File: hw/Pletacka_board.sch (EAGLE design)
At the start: 52 parts, among them U1 LM75BDP-NEW, U2 EL357N(A)(TA)-G, U3 EL357N(A)(TA)-G, U4 EL357N(A)(TA)-G, U5 EL357N(A)(TA)-G, U6 TPS54231D

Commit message: Start fixing
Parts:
- C1: LCSC_ID (none) -> C13585; LSCS_ID C13585 -> (none)
- D6: LCSC_ID (none) -> C8598; LSCS_ID C8598 -> (none)
- R10, R12, R8: LCSC_ID (none) -> C17944; LSCS_ID C17944 -> (none)

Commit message: Fix all atributes (fix #12)
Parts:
- D1, D2, D4: LCSC_ID (none) -> C8598; LSCS_ID C8598 -> (none)
- R11, R13, R7, R9: LCSC_ID (none) -> C25804; LSCS_ID C25804 -> (none)
- R15: LCSC_ID (none) -> C22818; LSCS_ID C22818 -> (none)
- R6: LCSC_ID (none) -> C17944; LSCS_ID C17944 -> (none)
- S1, S2: LCSC_ID (none) -> C318888
- U$2: LCSC_ID (none) -> C169399
- U2: LCSC_ID (none) -> C6649; LSCS_ID C6649 -> (none)
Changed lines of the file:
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@@
 <part name="CON1" library="#Svorkovnice" deviceset="AK500/2" device=""/>
 <part name="R6" library="rcl_upravena" deviceset="R-EU_" device="R1206" value="2k/0.25W">
-<attribute name="LSCS_ID" value="C17944"/>
+<attribute name="LCSC_ID" value="C17944"/>
 </part>
 <part name="GND6" library="supply1" library_urn="urn:adsk.eagle:library:371" deviceset="GND" device=""/>
 <part name="R7" library="rcl_upravena" deviceset="R-EU_" device="R0603" value="10k">
-<attribute name="LSCS_ID" value="C25804"/>
+<attribute name="LCSC_ID" value="C25804"/>
 </part>
 <part name="+3V3" library="supply1" library_urn="urn:adsk.eagle:library:371" deviceset="+3V3" device=""/>
@@
 <part name="GND7" library="supply1" library_urn="urn:adsk.eagle:library:371" deviceset="GND" device=""/>
 <part name="R9" library="rcl_upravena" deviceset="R-EU_" device="R0603" value="10k">
-<attribute name="LSCS_ID" value="C25804"/>
+<attribute name="LCSC_ID" value="C25804"/>
 </part>
 <part name="+3V4" library="supply1" library_urn="urn:adsk.eagle:library:371" deviceset="+3V3" device=""/>
@@
 <part name="GND8" library="supply1" library_urn="urn:adsk.eagle:library:371" deviceset="GND" device=""/>
 <part name="R11" library="rcl_upravena" deviceset="R-EU_" device="R0603" value="10k">
-<attribute name="LSCS_ID" value="C25804"/>
+<attribute name="LCSC_ID" value="C25804"/>
 </part>
 <part name="+3V5" library="supply1" library_urn="urn:adsk.eagle:library:371" deviceset="+3V3" device=""/>
@@
 <part name="GND9" library="supply1" library_urn="urn:adsk.eagle:library:371" deviceset="GND" device=""/>
 <part name="R13" library="rcl_upravena" deviceset="R-EU_" device="R0603" value="10k">
-<attribute name="LSCS_ID" value="C25804"/>
+<attribute name="LCSC_ID" value="C25804"/>
 </part>
 <part name="+3V6" library="supply1" library_urn="urn:adsk.eagle:library:371" deviceset="+3V3" device=""/>
 <part name="U2" library="EL357N_A__TA_-G" deviceset="EL357N(A)(TA)-G" device="">
-<attribute name="LSCS_ID" value="C6649"/>
+<attribute name="LCSC_ID" value="C6649"/>
 </part>
 <part name="U3" library="EL357N_A__TA_-G" deviceset="EL357N(A)(TA)-G" device="">
@@
 </pinmapping>
 </spice>
-<attribute name="LSCS_ID" value="C22818"/>
+<attribute name="LCSC_ID" value="C22818"/>
 </part>
 <part name="C2" library="rcl_upravena" deviceset="C-EU" device="C0603" value="10p">
@@
 <attribute name="LCSC_ID" value="C2286"/>
 </part>
-<part name="U$2" library="SWRB1204S-680MT" deviceset="SWRB1204S" device=""/>
+<part name="U$2" library="SWRB1204S-680MT" deviceset="SWRB1204S" device="">
+<attribute name="LCSC_ID" value="C169399"/>
+</part>
 <part name="GND12" library="supply1" library_urn="urn:adsk.eagle:library:371" deviceset="GND" device=""/>
-<part name="S1" library="switch-omron" deviceset="10-XX" device="_SMD" value="CHOOSE_ME"/>
-<part name="S2" library="switch-omron" deviceset="10-XX" device="_SMD" value="CHOOSE_ME"/>
+<part name="S1" library="switch-omron" deviceset="10-XX" device="_SMD" value="CHOOSE_ME">
+<attribute name="LCSC_ID" value="C318888"/>
+</part>
+<part name="S2" library="switch-omron" deviceset="10-XX" device="_SMD" value="CHOOSE_ME">
+<attribute name="LCSC_ID" value="C318888"/>
+</part>
 <part name="GND2" library="supply1" library_urn="urn:adsk.eagle:library:371" deviceset="GND" device=""/>
 <part name="+3V7" library="supply1" library_urn="urn:adsk.eagle:library:371" deviceset="+3V3" device=""/>
@@
 </part>
 <part name="D1" library="B5819W" deviceset="B5819W" device="">
-<attribute name="LSCS_ID" value="C8598"/>
+<attribute name="LCSC_ID" value="C8598"/>
 </part>
 <part name="D2" library="B5819W" deviceset="B5819W" device="">
-<attribute name="LSCS_ID" value="C8598"/>
+<attribute name="LCSC_ID" value="C8598"/>
 </part>
 <part name="D4" library="B5819W" deviceset="B5819W" device="">
-<attribute name="LSCS_ID" value="C8598"/>
+<attribute name="LCSC_ID" value="C8598"/>
 </part>
 </parts>
@@
 <instance part="S1" gate="1" x="208.28" y="91.44" smashed="yes" rot="MR270">
 <attribute name="NAME" x="208.28" y="96.52" size="1.27" layer="95" rot="R180" align="top-center"/>
+<attribute name="LCSC_ID" x="208.28" y="91.44" size="1.778" layer="96" rot="MR270" display="off"/>
 </instance>
 <instance part="S2" gate="1" x="208.28" y="60.96" smashed="yes" rot="MR270">
 <attribute name="NAME" x="208.28" y="66.04" size="1.27" layer="95" rot="R180" align="top-center"/>
+<attribute name="LCSC_ID" x="208.28" y="60.96" size="1.778" layer="96" rot="MR270" display="off"/>
 </instance>
 <instance part="GND2" gate="1" x="96.52" y="43.18" smashed="yes" rot="R270">
@@
 <attribute name="NAME" x="29.21" y="151.3586" size="1.778" layer="95"/>
 <attribute name="VALUE" x="29.21" y="146.558" size="1.778" layer="96"/>
-<attribute name="LSCS_ID" x="33.02" y="149.86" size="1.778" layer="96" display="off"/>
+<attribute name="LCSC_ID" x="33.02" y="149.86" size="1.778" layer="96" display="off"/>
 </instance>
 <instance part="GND6" gate="1" x="76.2" y="139.7" smashed="yes">
@@
 <attribute name="NAME" x="74.7014" y="153.67" size="1.778" layer="95" rot="R90"/>
 <attribute name="VALUE" x="79.502" y="153.67" size="1.778" layer="96" rot="R90"/>
-<attribute name="LSCS_ID" x="76.2" y="157.48" size="1.778" layer="96" rot="R90" display="off"/>
+<attribute name="LCSC_ID" x="76.2" y="157.48" size="1.778" layer="96" rot="R90" display="off"/>
 </instance>
 <instance part="+3V3" gate="G$1" x="76.2" y="165.1" smashed="yes">
@@
 <attribute name="NAME" x="74.7014" y="115.57" size="1.778" layer="95" rot="R90"/>
 <attribute name="VALUE" x="79.502" y="115.57" size="1.778" layer="96" rot="R90"/>
-<attribute name="LSCS_ID" x="76.2" y="119.38" size="1.778" layer="96" rot="R90" display="off"/>
+<attribute name="LCSC_ID" x="76.2" y="119.38" size="1.778" layer="96" rot="R90" display="off"/>
 </instance>
 <instance part="+3V4" gate="G$1" x="76.2" y="127" smashed="yes">
@@
 <attribute name="NAME" x="74.7014" y="74.93" size="1.778" layer="95" rot="R90"/>
 <attribute name="VALUE" x="79.502" y="74.93" size="1.778" layer="96" rot="R90"/>
-<attribute name="LSCS_ID" x="76.2" y="78.74" size="1.778" layer="96" rot="R90" display="off"/>
+<attribute name="LCSC_ID" x="76.2" y="78.74" size="1.778" layer="96" rot="R90" display="off"/>
 </instance>
 <instance part="+3V5" gate="G$1" x="76.2" y="86.36" smashed="yes">
@@
 <attribute name="NAME" x="74.7014" y="29.21" size="1.778" layer="95" rot="R90"/>
 <attribute name="VALUE" x="79.502" y="29.21" size="1.778" layer="96" rot="R90"/>
-<attribute name="LSCS_ID" x="76.2" y="33.02" size="1.778" layer="96" rot="R90" display="off"/>
+<attribute name="LCSC_ID" x="76.2" y="33.02" size="1.778" layer="96" rot="R90" display="off"/>
 </instance>
 <instance part="+3V6" gate="G$1" x="76.2" y="40.64" smashed="yes">
@@
 <attribute name="NAME" x="50.7743" y="153.413590625" size="2.08636875" layer="95" ratio="10" rot="SR0"/>
 <attribute name="VALUE" x="50.77441875" y="138.216059375" size="2.087890625" layer="96" ratio="10" rot="SR0"/>
-<attribute name="LSCS_ID" x="58.42" y="147.32" size="1.778" layer="96" display="off"/>
+<attribute name="LCSC_ID" x="58.42" y="147.32" size="1.778" layer="96" display="off"/>
 </instance>
 <instance part="U3" gate="G$1" x="58.42" y="109.22" smashed="yes">
@@
 <attribute name="NAME" x="42.6974" y="111.76" size="1.778" layer="95" rot="R90"/>
 <attribute name="VALUE" x="45.4914" y="111.76" size="1.778" layer="96" rot="R90"/>
-<attribute name="LSCS_ID" x="43.18" y="109.22" size="1.778" layer="96" rot="R90" display="off"/>
+<attribute name="LCSC_ID" x="43.18" y="109.22" size="1.778" layer="96" rot="R90" display="off"/>
 </instance>
 <instance part="D2" gate="G$1" x="43.18" y="68.58" smashed="yes" rot="R90">
 <attribute name="NAME" x="42.6974" y="71.12" size="1.778" layer="95" rot="R90"/>
 <attribute name="VALUE" x="45.4914" y="71.12" size="1.778" layer="96" rot="R90"/>
-<attribute name="LSCS_ID" x="43.18" y="68.58" size="1.778" layer="96" rot="R90" display="off"/>
+<attribute name="LCSC_ID" x="43.18" y="68.58" size="1.778" layer="96" rot="R90" display="off"/>
 </instance>
 <instance part="D4" gate="G$1" x="43.18" y="22.86" smashed="yes" rot="R90">
 <attribute name="NAME" x="42.6974" y="25.4" size="1.778" layer="95" rot="R90"/>
 <attribute name="VALUE" x="45.4914" y="25.4" size="1.778" layer="96" rot="R90"/>
-<attribute name="LSCS_ID" x="43.18" y="22.86" size="1.778" layer="96" rot="R90" display="off"/>
+<attribute name="LCSC_ID" x="43.18" y="22.86" size="1.778" layer="96" rot="R90" display="off"/>
 </instance>
 </instances>
@@
 <attribute name="NAME" x="72.1614" y="74.93" size="1.778" layer="95" rot="R90"/>
 <attribute name="VALUE" x="76.962" y="74.93" size="1.778" layer="96" rot="R90"/>
-<attribute name="LSCS_ID" x="73.66" y="78.74" size="1.778" layer="96" rot="R90" display="off"/>
+<attribute name="LCSC_ID" x="73.66" y="78.74" size="1.778" layer="96" rot="R90" display="off"/>
 </instance>
 <instance part="C2" gate="G$1" x="86.36" y="63.5" smashed="yes">
@@
 <attribute name="LCSC_ID" x="111.76" y="63.5" size="1.778" layer="96" display="off"/>
 </instance>
-<instance part="U$2" gate="G$1" x="208.28" y="83.82" smashed="yes"/>
+<instance part="U$2" gate="G$1" x="208.28" y="83.82" smashed="yes">
+<attribute name="LCSC_ID" x="208.28" y="83.82" size="1.778" layer="96" display="off"/>
+</instance>
 <instance part="D3" gate="G$1" x="190.5" y="96.52" smashed="yes" rot="R270">
 <attribute name="NAME" x="192.405" y="98.806" size="1.27" layer="95" rot="R270"/>

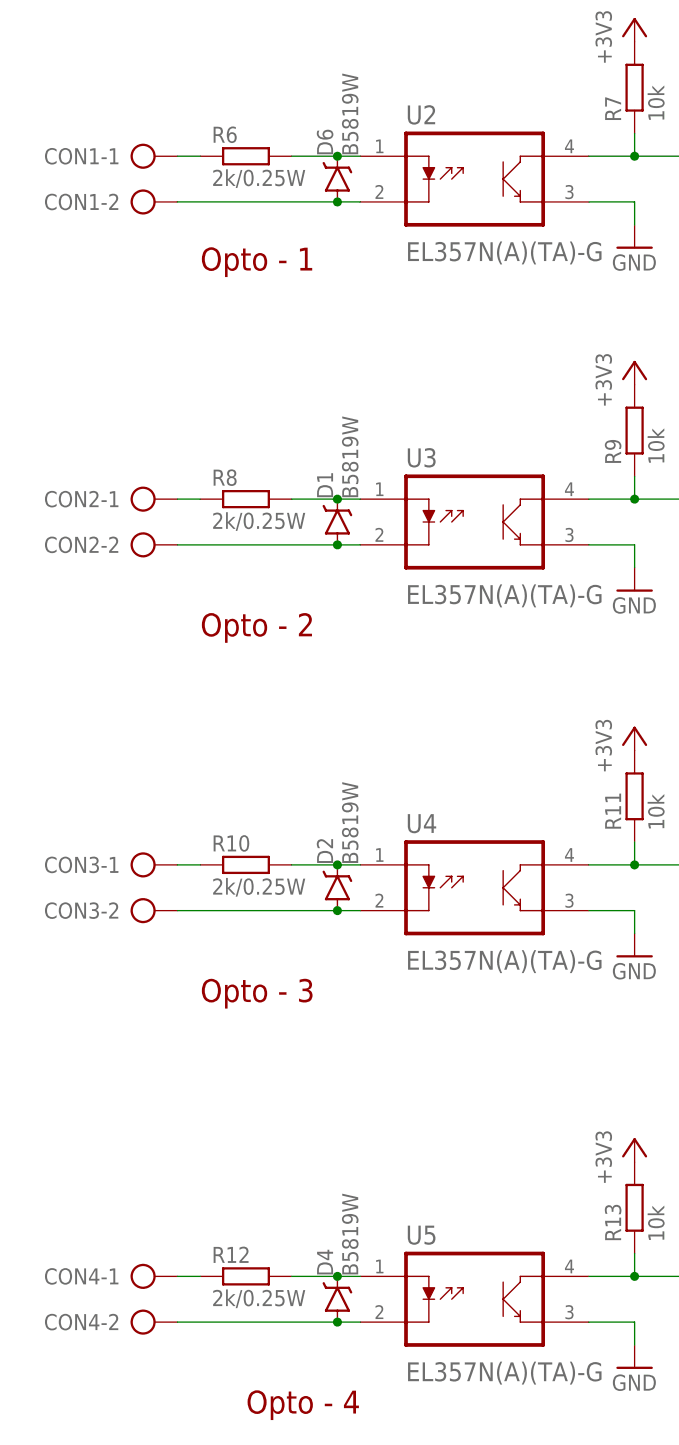
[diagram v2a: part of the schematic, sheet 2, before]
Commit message: Change octocoupler resistor to 20k (close #2)
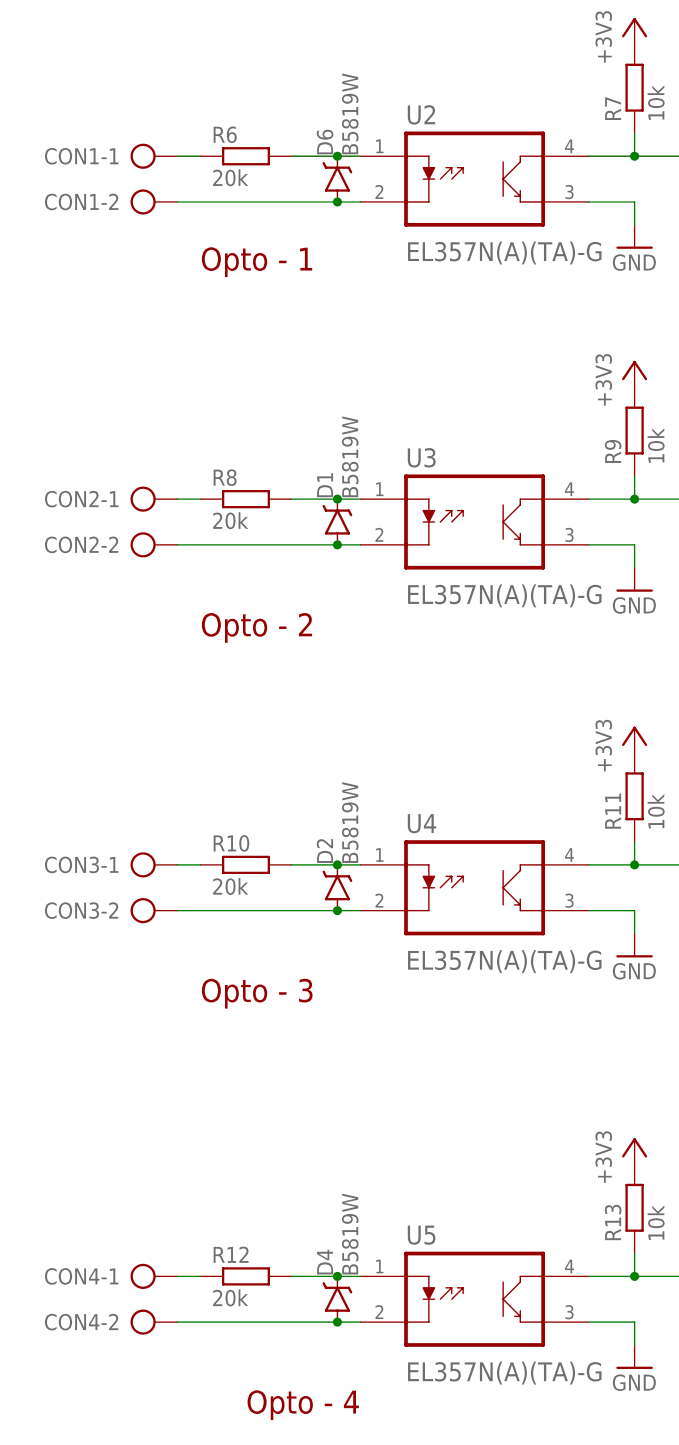
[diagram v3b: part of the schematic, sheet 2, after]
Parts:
- R10, R12, R6, R8: value 2k/0.25W -> 20k; device rcl_upravena:R-EU_R1206 -> rcl_upravena:R-EU_R0603; LCSC_ID C17944 -> C4184

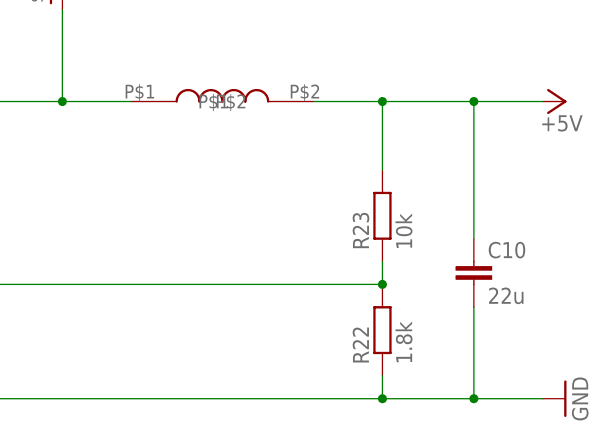
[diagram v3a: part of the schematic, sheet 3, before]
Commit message: Change step-down voltage (close #4)
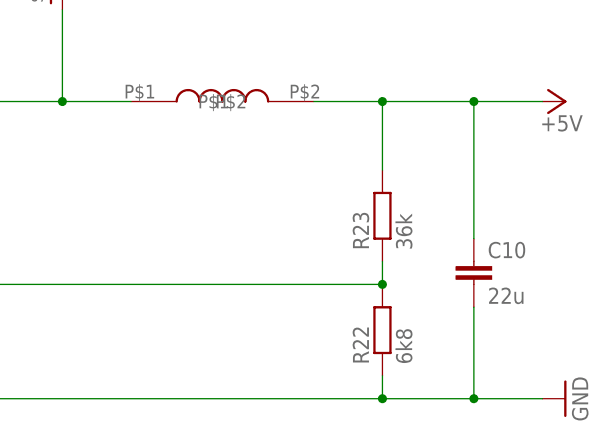
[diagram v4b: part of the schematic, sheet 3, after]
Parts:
- R22: value 1.8k -> 6k8; LCSC_ID C4177 -> C23212
- R23: value 10k -> 36k; LCSC_ID C25804 -> C23147
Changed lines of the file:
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@@
 <attribute name="LCSC_ID" value="C59461"/>
 </part>
-<part name="R22" library="rcl_upravena" deviceset="R-EU_" device="R0603" value="1.8k">
+<part name="R22" library="rcl_upravena" deviceset="R-EU_" device="R0603" value="6k8">
 <spice>
 <pinmapping spiceprefix="R">
@@
 </pinmapping>
 </spice>
-<attribute name="LCSC_ID" value="C4177"/>
+<attribute name="LCSC_ID" value="C23212"/>
 </part>
-<part name="R23" library="rcl_upravena" deviceset="R-EU_" device="R0603" value="10k">
+<part name="R23" library="rcl_upravena" deviceset="R-EU_" device="R0603" value="36k">
 <spice>
 <pinmapping spiceprefix="R">
@@
 </pinmapping>
 </spice>
-<attribute name="LCSC_ID" value="C25804"/>
+<attribute name="LCSC_ID" value="C23147"/>
 </part>
 <part name="C11" library="rcl_upravena" deviceset="C-EU" device="C0603" value="100n">

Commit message: Change package of capacitor to 0805 (close #3)
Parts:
- C10: device rcl_upravena:C-EUC0603 -> rcl_upravena:C-EUC0805; LCSC_ID C59461 -> C45783
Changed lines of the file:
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@@
 <part name="P+3" library="supply1" library_urn="urn:adsk.eagle:library:371" deviceset="+5V" device=""/>
 <part name="GND10" library="supply1" library_urn="urn:adsk.eagle:library:371" deviceset="GND" device=""/>
-<part name="C10" library="rcl_upravena" deviceset="C-EU" device="C0603" value="22u">
-<attribute name="LCSC_ID" value="C59461"/>
+<part name="C10" library="rcl_upravena" deviceset="C-EU" device="C0805" value="22u">
+<attribute name="LCSC_ID" value="C45783"/>
 </part>
 <part name="R22" library="rcl_upravena" deviceset="R-EU_" device="R0603" value="6k8">

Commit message: Edit buttons lables (close #16)
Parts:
- B0: value CHOOSE_ME -> ENTER
- B1: value CHOOSE_ME -> B1
- renumbered S1 to B0, S2 to B1
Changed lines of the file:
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@@
 </part>
 <part name="GND12" library="supply1" library_urn="urn:adsk.eagle:library:371" deviceset="GND" device=""/>
-<part name="S1" library="switch-omron" deviceset="10-XX" device="_SMD" value="CHOOSE_ME">
+<part name="B0" library="switch-omron" deviceset="10-XX" device="_SMD" value="ENTER">
 <attribute name="LCSC_ID" value="C318888"/>
 </part>
-<part name="S2" library="switch-omron" deviceset="10-XX" device="_SMD" value="CHOOSE_ME">
+<part name="B1" library="switch-omron" deviceset="10-XX" device="_SMD" value="B1">
 <attribute name="LCSC_ID" value="C318888"/>
 </part>
@@
 <attribute name="VALUE" x="215.9" y="73.66" size="1.778" layer="96"/>
 </instance>
-<instance part="S1" gate="1" x="208.28" y="91.44" smashed="yes" rot="MR270">
+<instance part="B0" gate="1" x="208.28" y="91.44" smashed="yes" rot="MR270">
 <attribute name="NAME" x="208.28" y="96.52" size="1.27" layer="95" rot="R180" align="top-center"/>
 <attribute name="LCSC_ID" x="208.28" y="91.44" size="1.778" layer="96" rot="MR270" display="off"/>
 </instance>
-<instance part="S2" gate="1" x="208.28" y="60.96" smashed="yes" rot="MR270">
+<instance part="B1" gate="1" x="208.28" y="60.96" smashed="yes" rot="MR270">
 <attribute name="NAME" x="208.28" y="66.04" size="1.27" layer="95" rot="R180" align="top-center"/>
 <attribute name="LCSC_ID" x="208.28" y="60.96" size="1.778" layer="96" rot="MR270" display="off"/>
@@
 <wire x1="187.96" y1="50.8" x2="218.44" y2="50.8" width="0.1524" layer="91"/>
 <junction x="218.44" y="50.8"/>
-<pinref part="S2" gate="1" pin="P"/>
-<pinref part="S2" gate="1" pin="P1"/>
+<pinref part="B1" gate="1" pin="P"/>
+<pinref part="B1" gate="1" pin="P1"/>
 </segment>
 <segment>
@@
 <junction x="218.44" y="81.28"/>
 <junction x="218.44" y="88.9"/>
-<pinref part="S1" gate="1" pin="P"/>
-<pinref part="S1" gate="1" pin="P1"/>
+<pinref part="B0" gate="1" pin="P"/>
+<pinref part="B0" gate="1" pin="P1"/>
 </segment>
 <segment>
@@
 <pinref part="C5" gate="G$1" pin="2"/>
 <junction x="187.96" y="91.44"/>
-<pinref part="S1" gate="1" pin="S"/>
-<pinref part="S1" gate="1" pin="S1"/>
+<pinref part="B0" gate="1" pin="S"/>
+<pinref part="B0" gate="1" pin="S1"/>
 </segment>
 </net>
@@
 <pinref part="C4" gate="G$1" pin="2"/>
 <junction x="187.96" y="60.96"/>
-<pinref part="S2" gate="1" pin="S"/>
-<pinref part="S2" gate="1" pin="S1"/>
-</segment>
-</net>
+<pinref part="B1" gate="1" pin="S"/>
+<pinref part="B1" gate="1" pin="S1"/>
+</segment>
+</net>

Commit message: Fix ON button schema name
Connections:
- net LED_POWER renamed LED_ON
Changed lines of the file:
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@@
-</segment>
-</net>
-<net name="LED_POWER" class="0">
-<segment>
-<pinref part="R1" gate="G$1" pin="1"/>
-<wire x1="190.5" y1="149.86" x2="185.42" y2="149.86" width="0.1524" layer="91"/>
-<label x="185.42" y="149.86" size="1.27" layer="95" rot="R180" xref="yes"/>
-</segment>
-<segment>
-<pinref part="U$1" gate="G$1" pin="25"/>
-<wire x1="83.82" y1="93.98" x2="88.9" y2="93.98" width="0.1524" layer="91"/>
-<label x="88.9" y="93.98" size="1.27" layer="95" xref="yes"/>
 </segment>
 </net>
@@
 </segment>
 </net>
+<net name="LED_ON" class="0">
+<segment>
+<pinref part="R1" gate="G$1" pin="1"/>
+<wire x1="190.5" y1="149.86" x2="185.42" y2="149.86" width="0.1524" layer="91"/>
+<label x="185.42" y="149.86" size="1.27" layer="95" rot="R180" xref="yes"/>
+</segment>
+<segment>
+<pinref part="U$1" gate="G$1" pin="25"/>
+<wire x1="83.82" y1="93.98" x2="88.9" y2="93.98" width="0.1524" layer="91"/>
+<label x="88.9" y="93.98" size="1.27" layer="95" xref="yes"/>
+</segment>
+</net>
